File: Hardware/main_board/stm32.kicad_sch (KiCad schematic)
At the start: 43 parts, among them J8 USB_C, U1 STM32WB55RGVx, Y1 32MHz, Y2 32.768K

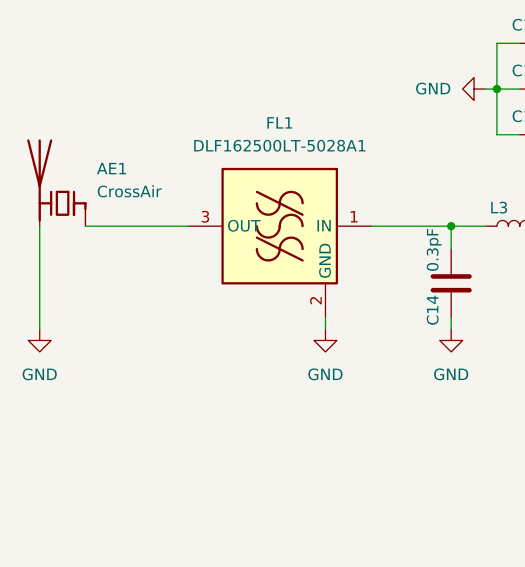
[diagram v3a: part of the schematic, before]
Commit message: sch: add more footprints
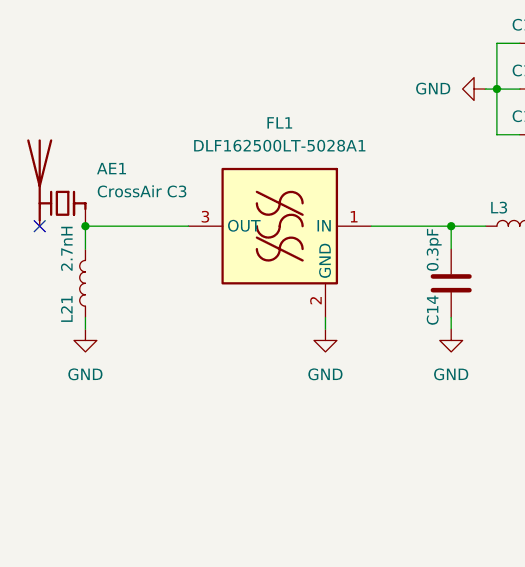
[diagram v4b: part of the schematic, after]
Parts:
- added L21: 2.7nH, Inductor_SMD:L_0402_1005Metric, symbol Device:L
- AE1: value CrossAir -> CrossAir C3; footprint (none) -> Library:CrossAir-C3
- J8: footprint (none) -> Connector_USB:USB_C_Receptacle_G-Switch_GT-USB-7010ASV
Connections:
- net GND: now also L21.1; no longer AE1.2 (PCB_Trace)
- net at AE1.1 (FEED), FL1.3 (OUT): now also L21.2
- no-connect marks 2 -> 3
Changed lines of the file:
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@@
 	)
 	(junction
+		(at 27.94 92.71)
+		(diameter 0)
+		(color 0 0 0 0)
+	)
+	(junction
 		(at 240.03 96.52)
 		(diameter 0)
@@
 	)
 	(no_connect
+		(at 22.86 92.71)
+	)
+	(no_connect
 		(at 241.3 106.68)
 	)
@@
 	(wire
 		(pts
-			(xy 22.86 92.71) (xy 22.86 104.14)
-		)
-		(stroke
-			(width 0)
-			(type default)
-		)
-	)
-	(wire
-		(pts
 			(xy 105.41 52.07) (xy 107.95 52.07)
 		)
@@
 	(wire
 		(pts
+			(xy 27.94 92.71) (xy 27.94 95.25)
+		)
+		(stroke
+			(width 0)
+			(type default)
+		)
+	)
+	(wire
+		(pts
 			(xy 68.58 92.71) (xy 59.69 92.71)
 		)
@@
 	(wire
 		(pts
+			(xy 27.94 102.87) (xy 27.94 104.14)
+		)
+		(stroke
+			(width 0)
+			(type default)
+		)
+	)
+	(wire
+		(pts
 			(xy 129.54 60.96) (xy 129.54 62.23)
 		)
@@
 	)
 	(symbol
+		(lib_id "Device:L")
+		(at 27.94 99.06 180)
+		(unit 1)
+		(exclude_from_sim no)
+		(in_bom yes)
+		(on_board yes)
+		(dnp no)
+		(property "Reference" "L21"
+			(at 26.67 100.33 90)
+			(effects
+				(font
+					(size 1.27 1.27)
+				)
+				(justify left top)
+			)
+		)
+		(property "Value" "2.7nH"
+			(at 26.67 97.79 90)
+			(effects
+				(font
+					(size 1.27 1.27)
+				)
+				(justify right top)
+			)
+		)
+		(property "Footprint" "Inductor_SMD:L_0402_1005Metric"
+			(at 27.94 99.06 0)
+			(effects
+				(font
+					(size 1.27 1.27)
+				)
+				(hide yes)
+			)
+		)
+		(property "Datasheet" "~"
+			(at 27.94 99.06 0)
+			(effects
+				(font
+					(size 1.27 1.27)
+				)
+				(hide yes)
+			)
+		)
+		(property "Description" "Inductor"
+			(at 27.94 99.06 0)
+			(effects
+				(font
+					(size 1.27 1.27)
+				)
+				(hide yes)
+			)
+		)
+		(pin "1"
+		)
+		(pin "2"
+		)
+		(instances
+			(project "main_board"
+				(path "/16216a68-6dea-41d7-8e15-2cc84f72f8e2/8225a072-bd5c-4ab0-988a-5acfd87a3b3a"
+					(reference "L21")
+					(unit 1)
+				)
+			)
+		)
+	)
+	(symbol
 		(lib_id "Device:R_Small_US")
 		(at 217.17 93.98 180)
@@
 			)
 		)
-		(property "Value" "CrossAir"
+		(property "Value" "CrossAir C3"
 			(at 29.21 88.8999 0)
 			(effects
@@
 			)
 		)
-		(property "Footprint" ""
+		(property "Footprint" "Library:CrossAir-C3"
 			(at 27.94 85.725 0)
 			(effects
@@
 	)
 	(symbol
+		(lib_id "power:GND")
+		(at 27.94 104.14 0)
+		(unit 1)
+		(exclude_from_sim no)
+		(in_bom yes)
+		(on_board yes)
+		(dnp no)
+		(fields_autoplaced yes)
+		(property "Reference" "#PWR0142"
+			(at 27.94 110.49 0)
+			(effects
+				(font
+					(size 1.27 1.27)
+				)
+				(hide yes)
+			)
+		)
+		(property "Value" "GND"
+			(at 27.94 109.22 0)
+			(effects
+				(font
+					(size 1.27 1.27)
+				)
+			)
+		)
+		(property "Footprint" ""
+			(at 27.94 104.14 0)
+			(effects
+				(font
+					(size 1.27 1.27)
+				)
+				(hide yes)
+			)
+		)
+		(property "Datasheet" ""
+			(at 27.94 104.14 0)
+			(effects
+				(font
+					(size 1.27 1.27)
+				)
+				(hide yes)
+			)
+		)
+		(property "Description" "Power symbol creates a global label with name \"GND\" , ground"
+			(at 27.94 104.14 0)
+			(effects
+				(font
+					(size 1.27 1.27)
+				)
+				(hide yes)
+			)
+		)
+		(pin "1"
+		)
+		(instances
+			(project "main_board"
+				(path "/16216a68-6dea-41d7-8e15-2cc84f72f8e2/8225a072-bd5c-4ab0-988a-5acfd87a3b3a"
+					(reference "#PWR0142")
+					(unit 1)
+				)
+			)
+		)
+	)
+	(symbol
 		(lib_id "Connector:TestPoint")
 		(at 158.75 95.25 270)
@@
 	)
 	(symbol
-		(lib_id "power:GND")
-		(at 22.86 104.14 0)
-		(unit 1)
-		(exclude_from_sim no)
-		(in_bom yes)
-		(on_board yes)
-		(dnp no)
-		(fields_autoplaced yes)
-		(property "Reference" "#PWR014"
-			(at 22.86 110.49 0)
-			(effects
-				(font
-					(size 1.27 1.27)
-				)
-				(hide yes)
-			)
-		)
-		(property "Value" "GND"
-			(at 22.86 109.22 0)
-			(effects
-				(font
-					(size 1.27 1.27)
-				)
-			)
-		)
-		(property "Footprint" ""
-			(at 22.86 104.14 0)
-			(effects
-				(font
-					(size 1.27 1.27)
-				)
-				(hide yes)
-			)
-		)
-		(property "Datasheet" ""
-			(at 22.86 104.14 0)
-			(effects
-				(font
-					(size 1.27 1.27)
-				)
-				(hide yes)
-			)
-		)
-		(property "Description" "Power symbol creates a global label with name \"GND\" , ground"
-			(at 22.86 104.14 0)
-			(effects
-				(font
-					(size 1.27 1.27)
-				)
-				(hide yes)
-			)
-		)
-		(pin "1"
-		)
-		(instances
-			(project "main_board"
-				(path "/16216a68-6dea-41d7-8e15-2cc84f72f8e2/8225a072-bd5c-4ab0-988a-5acfd87a3b3a"
-					(reference "#PWR014")
-					(unit 1)
-				)
-			)
-		)
-	)
-	(symbol
 		(lib_id "Device:C")
 		(at 57.15 44.45 180)
@@
 			)
 		)
-		(property "Footprint" ""
+		(property "Footprint" "Connector_USB:USB_C_Receptacle_G-Switch_GT-USB-7010ASV"
 			(at 252.73 93.98 0)
 			(effects
@@
 			)
 		)
-		(property "Datasheet" ""
+		(property "Datasheet" "https://product.tdk.com/system/files/dam/doc/product/rf/rf/filter/catalog/rf_lpf_dlf162500lt-5028a1_en.pdf"
 			(at 49.53 85.09 0)
 			(effects

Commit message: layout: change some of the footprint and start to layout
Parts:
- FL1: footprint (none) -> Library:DLF162500LT
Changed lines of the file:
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@@
 			)
 		)
-		(property "Footprint" ""
+		(property "Footprint" "Library:DLF162500LT"
 			(at 49.53 85.09 0)
 			(effects

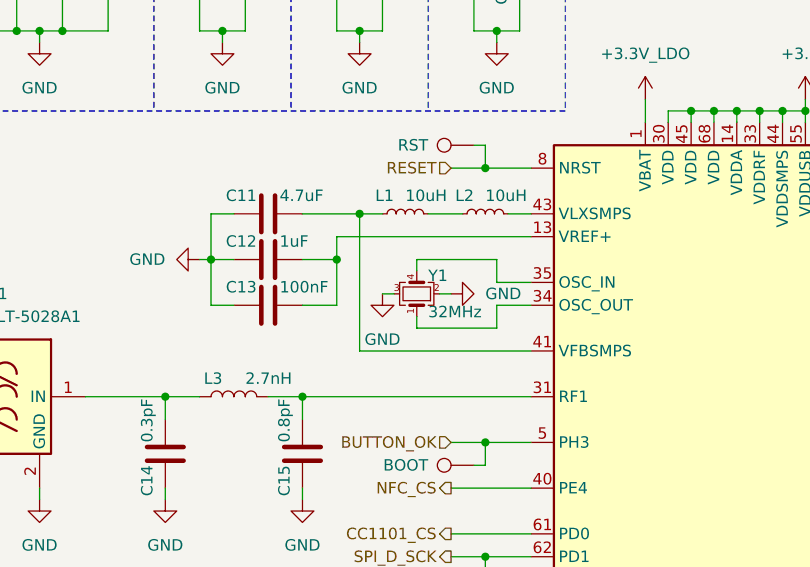
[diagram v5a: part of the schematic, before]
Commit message: layout: finish the Sub-1G filter
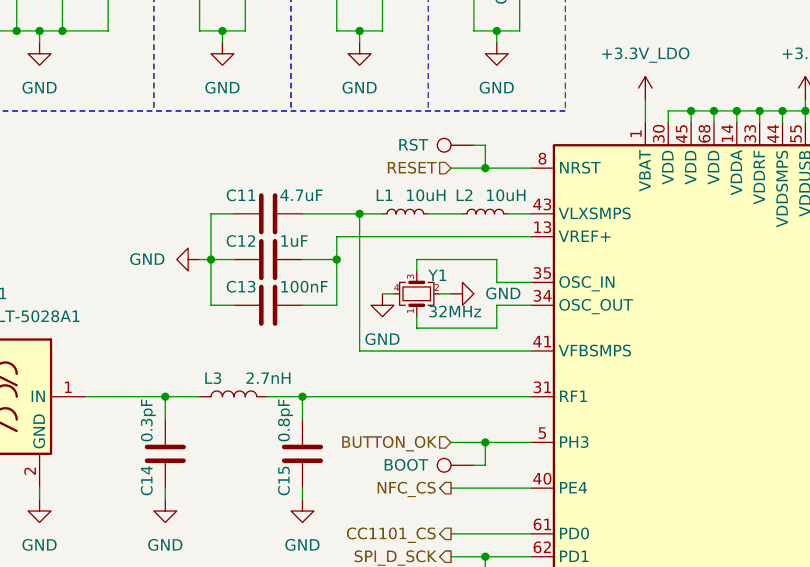
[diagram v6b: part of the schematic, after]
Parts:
- Y1: symbol Device:Crystal_GND23_Small -> Device:Crystal_GND24_Small
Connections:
- net GND: now also Y1.4; no longer Y1.3
- net at U1.35 (OSC_IN): now also Y1.3; no longer Y1.4
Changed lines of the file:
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@@
 	)
 	(symbol
-		(lib_id "Device:Crystal_GND23_Small")
+		(lib_id "Device:Crystal_GND24_Small")
 		(at 96.52 81.28 90)
 		(unit 1)
@@
 			)
 		)
-		(property "Description" "Four pin crystal, GND on pins 2 and 3, small symbol"
+		(property "Description" "Four pin crystal, GND on pins 2 and 4, small symbol"
 			(at 96.52 81.28 0)
 			(effects

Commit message: layout: optimise cc1101 and start the stm32
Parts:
- C14, C15: footprint Capacitor_SMD:C_0402_1005Metric -> Capacitor_SMD:C_0201_0603Metric
- L21, L3: footprint Inductor_SMD:L_0402_1005Metric -> Inductor_SMD:L_0201_0603Metric
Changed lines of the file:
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@@
 			)
 		)
-		(property "Footprint" "Capacitor_SMD:C_0402_1005Metric"
+		(property "Footprint" "Capacitor_SMD:C_0201_0603Metric"
 			(at 67.6148 95.25 0)
 			(effects
@@
 			)
 		)
-		(property "Footprint" "Inductor_SMD:L_0402_1005Metric"
+		(property "Footprint" "Inductor_SMD:L_0201_0603Metric"
 			(at 27.94 99.06 0)
 			(effects
@@
 			)
 		)
-		(property "Footprint" "Capacitor_SMD:C_0402_1005Metric"
+		(property "Footprint" "Capacitor_SMD:C_0201_0603Metric"
 			(at 82.8548 95.25 0)
 			(effects
@@
 			)
 		)
-		(property "Footprint" "Inductor_SMD:L_0402_1005Metric"
+		(property "Footprint" "Inductor_SMD:L_0201_0603Metric"
 			(at 76.2 92.71 0)
 			(effects

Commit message: layout: layout some of SMPSs
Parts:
- L1: footprint Inductor_SMD:L_0805_2012Metric -> Inductor_SMD:L_0603_1608Metric
- Y2: footprint Crystal:Crystal_SMD_2012-2Pin_2.0x1.2mm -> Crystal:Crystal_SMD_3215-2Pin_3.2x1.5mm
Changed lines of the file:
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@@
 			)
 		)
-		(property "Footprint" "Crystal:Crystal_SMD_2012-2Pin_2.0x1.2mm"
+		(property "Footprint" "Crystal:Crystal_SMD_3215-2Pin_3.2x1.5mm"
 			(at 71.12 144.78 0)
 			(effects
@@
 			)
 		)
-		(property "Footprint" "Inductor_SMD:L_0805_2012Metric"
+		(property "Footprint" "Inductor_SMD:L_0603_1608Metric"
 			(at 95.25 72.39 0)
 			(effects
